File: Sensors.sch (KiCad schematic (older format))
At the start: 5 parts, among them U5 MPRLS0015PA000

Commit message: Correct schematics after review
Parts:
- added C13, C16, C17: 0.1uF, symbol Device:C_Small
- added C14: 1nF, symbol Device:C_Small
- added CONN10: Digital input 1, Molex Picoblade 2 pin, symbol _connectors:CONN_2PIN
- added CONN11: Digital input 2, Molex Picoblade 2 pin, symbol _connectors:CONN_2PIN
- added R6, R7, R8, R9: 10k, symbol Device:R_Small
- added TP1: TestPoint I2C_SDA, symbol Connector:TestPoint
- added TP2: TestPoint I2C_SCL, symbol Connector:TestPoint
- added U6: MPRLS0015PA000, MODULE, symbol _sensors:MPRLS0015PA000
- CONN7, CONN8: value ADC_2PIN -> ADC_2PIN, Molex Picoblade 2 pin
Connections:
- net labels added: DIGITAL_IN1, DIGITAL_IN2, VACUUM_SENS1_RESET, VACUUM_SENS2_RESET
- net labels removed: VACUUM_SENS_RST
- wire segments 9 -> 51
- no-connect marks 5 -> 10
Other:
- note added: "Fc = 318 Hz\n(10k+10k)/(10k*10k*100nF*2*pi)"
- moved on the sheet: C11, C12, CONN7, CONN8, U5

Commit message: Cleanup labels, motor placement, power labels
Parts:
- removed TP1: TestPoint I2C_SDA, symbol Connector:TestPoint
- removed TP2: TestPoint I2C_SCL, symbol Connector:TestPoint
- CONN10, CONN11: symbol _connectors:CONN_2PIN -> actuator-board-rescue:CONN_2PIN-_connectors
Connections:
- net labels added: GND, VCC
- net labels removed: SENSORS_GND, SENSORS_POWER
- wire segments 51 -> 42
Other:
- moved on the sheet: C11, C13, C16, C17, CONN7, CONN8, R6, R7, R8, R9

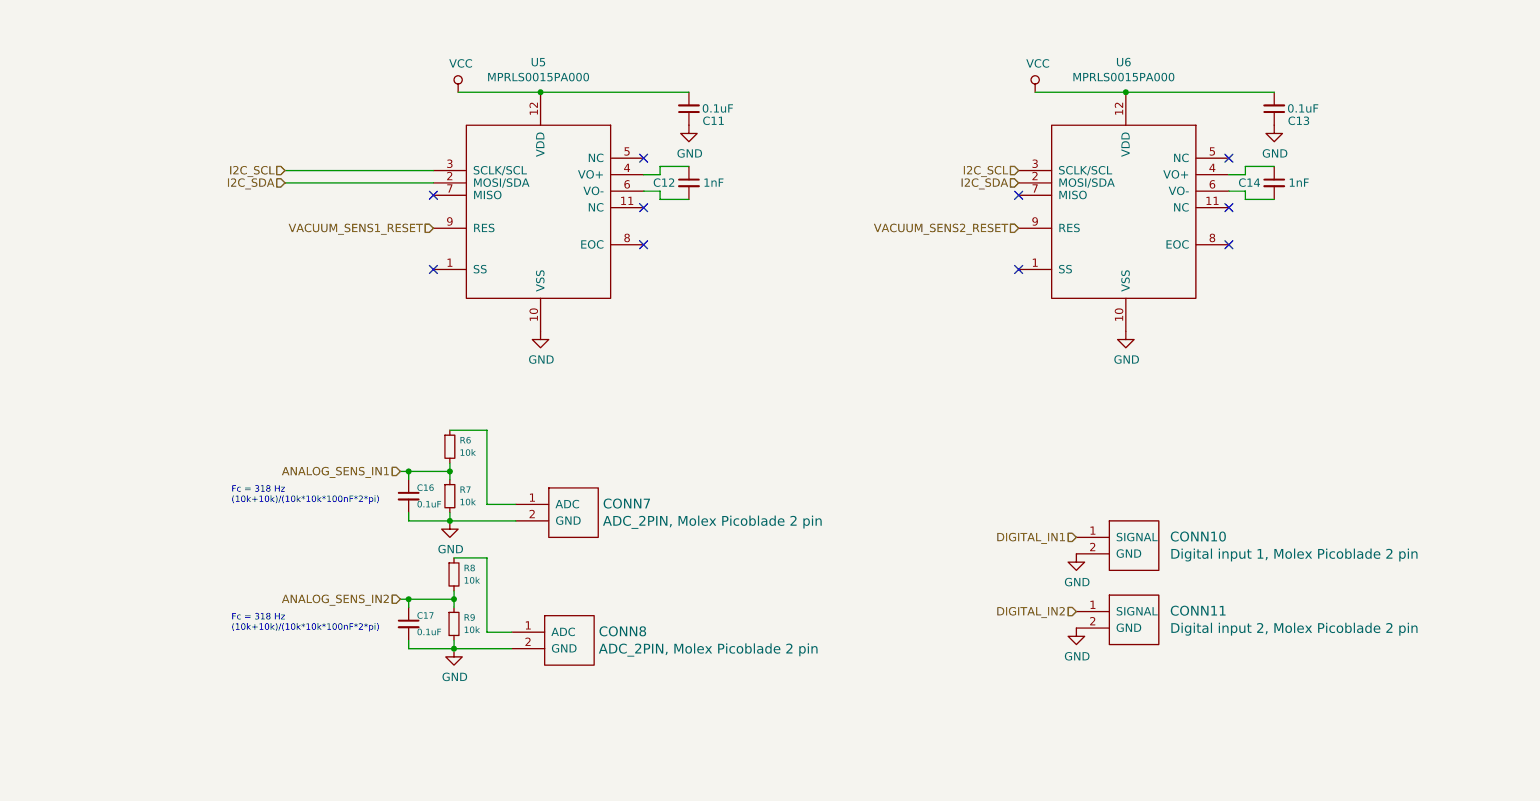
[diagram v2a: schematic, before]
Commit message: Clear component annotation
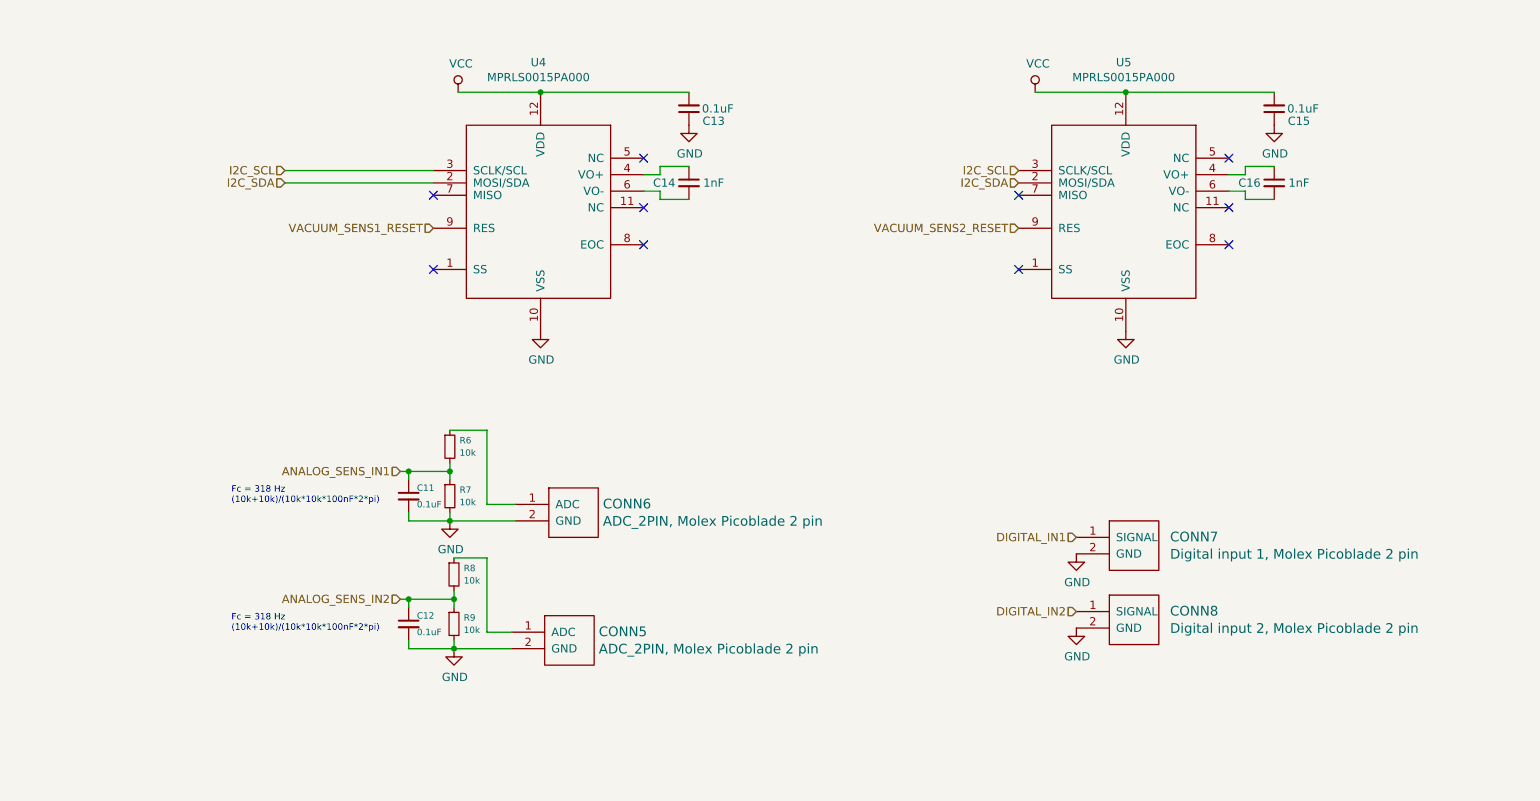
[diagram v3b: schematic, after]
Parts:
- renumbered C16 to C11, C17 to C12, C11 to C13, C12 to C14, C13 to C15, C14 to C16, CONN8 to CONN5, CONN7 to CONN6, CONN10 to CONN7, CONN11 to CONN8, U5 to U4, U6 to U5
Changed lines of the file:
@@
 NoConn ~ 3550 3125
 $Comp
-L Device:C_Small C12
+L Device:C_Small C14
 U 1 1 5E251FA3
 P 5100 2600
-F 0 "C12" H 4950 2600 50  0000 C CNN
+F 0 "C14" H 4950 2600 50  0000 C CNN
 F 1 "1nF" H 5250 2600 50  0000 C CNN
 F 2 "" H 5100 2600 50  0001 C CNN
@@
 NoConn ~ 4825 2975
 $Comp
-L _connectors:ADC_2PIN CONN8
+L _connectors:ADC_2PIN CONN5
 U 1 1 5E2563B4
 P 4375 5725
-F 0 "CONN8" H 4553 6128 59  0000 L CNN
+F 0 "CONN5" H 4553 6128 59  0000 L CNN
 F 1 "ADC_2PIN, Molex Picoblade 2 pin" H 4553 6023 59  0000 L CNN
 F 2 "" H 4375 5725 59  0000 C CNN
@@
 DIGITAL_IN1
 $Comp
-L actuator-board-rescue:CONN_2PIN-_connectors CONN11
+L actuator-board-rescue:CONN_2PIN-_connectors CONN?
 U 1 1 5E2B70AE
 P 7800 5600
-AR Path="/5E2B70AE" Ref="CONN11"  Part="1"
-AR Path="/5E1FAFCF/5E2B70AE" Ref="CONN11"  Part="1"
-F 0 "CONN11" H 8018 6003 59  0000 L CNN
+AR Path="/5E2B70AE" Ref="CONN?"  Part="1"
+AR Path="/5E1FAFCF/5E2B70AE" Ref="CONN8"  Part="1"
+F 0 "CONN8" H 8018 6003 59  0000 L CNN
 F 1 "Digital input 2, Molex Picoblade 2 pin" H 8018 5898 59  0000 L CNN
 F 2 "" H 7800 5600 59  0000 C CNN
@@
 NoConn ~ 7100 3125
 $Comp
-L Device:C_Small C14
+L Device:C_Small C16
 U 1 1 5E2C4BE4
 P 8650 2600
-F 0 "C14" H 8500 2600 50  0000 C CNN
+F 0 "C16" H 8500 2600 50  0000 C CNN
 F 1 "1nF" H 8800 2600 50  0000 C CNN
 F 2 "" H 8650 2600 50  0001 C CNN
@@
 	4200 2050 3700 2050
 $Comp
-L actuator-board-rescue:CONN_2PIN-_connectors CONN10
+L actuator-board-rescue:CONN_2PIN-_connectors CONN?
 U 1 1 5E2B60FB
 P 7800 5150
-AR Path="/5E2B60FB" Ref="CONN10"  Part="1"
-AR Path="/5E1FAFCF/5E2B60FB" Ref="CONN10"  Part="1"
-F 0 "CONN10" H 8018 5553 59  0000 L CNN
+AR Path="/5E2B60FB" Ref="CONN?"  Part="1"
+AR Path="/5E1FAFCF/5E2B60FB" Ref="CONN7"  Part="1"
+F 0 "CONN7" H 8018 5553 59  0000 L CNN
 F 1 "Digital input 1, Molex Picoblade 2 pin" H 8018 5448 59  0000 L CNN
 F 2 "" H 7800 5150 59  0000 C CNN
@@
 $EndComp
 $Comp
-L _sensors:MPRLS0015PA000 U5
+L _sensors:MPRLS0015PA000 U4
 U 1 1 5E2431FF
 P 4200 2850
-F 0 "U5" H 4187 3831 50  0000 C CNN
+F 0 "U4" H 4187 3831 50  0000 C CNN
 F 1 "MPRLS0015PA000" H 4187 3740 50  0000 C CNN
 F 2 "MODULE" H 4300 2200 50  0001 L CNN
@@
 $EndComp
 $Comp
-L Device:C_Small C13
+L Device:C_Small C15
 U 1 1 5E3021F3
 P 8650 2150
-F 0 "C13" H 8500 2225 50  0000 C CNN
+F 0 "C15" H 8500 2225 50  0000 C CNN
 F 1 "0.1uF" H 8475 2150 50  0000 C CNN
 F 2 "" H 8650 2150 50  0001 C CNN
@@
 $EndComp
 $Comp
-L Device:C_Small C16
+L Device:C_Small C11
 U 1 1 5E30FCAA
 P 3400 4500
-F 0 "C16" H 3450 4550 39  0000 L CNN
+F 0 "C11" H 3450 4550 39  0000 L CNN
 F 1 "0.1uF" H 3450 4450 39  0000 L CNN
 F 2 "" H 3400 4500 50  0001 C CNN
@@
 $EndComp
 $Comp
-L Device:C_Small C17
+L Device:C_Small C12
 U 1 1 5E315BCA
 P 3400 5275
-F 0 "C17" H 3450 5325 39  0000 L CNN
+F 0 "C12" H 3450 5325 39  0000 L CNN
 F 1 "0.1uF" H 3450 5225 39  0000 L CNN
 F 2 "" H 3400 5275 50  0001 C CNN
@@
 $EndComp
 $Comp
-L _connectors:ADC_2PIN CONN7
+L _connectors:ADC_2PIN CONN6
 U 1 1 5E255B96
 P 4400 4950
-F 0 "CONN7" H 4578 5353 59  0000 L CNN
+F 0 "CONN6" H 4578 5353 59  0000 L CNN
 F 1 "ADC_2PIN, Molex Picoblade 2 pin" H 4578 5248 59  0000 L CNN
 F 2 "" H 4400 4950 59  0000 C CNN
@@
 	3400 5125 3675 5125
 $Comp
-L power:VCC #PWR0104
+L power:VCC #PWR025
 U 1 1 5E4E3256
 P 3700 2050
-F 0 "#PWR0104" H 3700 1900 50  0001 C CNN
+F 0 "#PWR025" H 3700 1900 50  0001 C CNN
 F 1 "VCC" H 3717 2223 50  0000 C CNN
 F 2 "" H 3700 2050 50  0001 C CNN
@@
 $EndComp
 $Comp
-L power:VCC #PWR0105
+L power:VCC #PWR028
 U 1 1 5E4E76D3
 P 7200 2050
-F 0 "#PWR0105" H 7200 1900 50  0001 C CNN
+F 0 "#PWR028" H 7200 1900 50  0001 C CNN
 F 1 "VCC" H 7217 2223 50  0000 C CNN
 F 2 "" H 7200 2050 50  0001 C CNN
@@
 $EndComp
 $Comp
-L power:GND #PWR0106
+L power:GND #PWR032
 U 1 1 5E4E8303
 P 8650 2250
-F 0 "#PWR0106" H 8650 2000 50  0001 C CNN
+F 0 "#PWR032" H 8650 2000 50  0001 C CNN
 F 1 "GND" H 8655 2077 50  0000 C CNN
 F 2 "" H 8650 2250 50  0001 C CNN
@@
 $EndComp
 $Comp
-L power:GND #PWR0108
+L power:GND #PWR027
 U 1 1 5E4F06AA
 P 5100 2250
-F 0 "#PWR0108" H 5100 2000 50  0001 C CNN
+F 0 "#PWR027" H 5100 2000 50  0001 C CNN
 F 1 "GND" H 5105 2077 50  0000 C CNN
 F 2 "" H 5100 2250 50  0001 C CNN
@@
 $EndComp
 $Comp
-L Device:C_Small C11
+L Device:C_Small C13
 U 1 1 5E250C7A
 P 5100 2150
-F 0 "C11" H 4950 2225 50  0000 C CNN
+F 0 "C13" H 4950 2225 50  0000 C CNN
 F 1 "0.1uF" H 4925 2150 50  0000 C CNN
 F 2 "" H 5100 2150 50  0001 C CNN
@@
 Connection ~ 4200 2050
 $Comp
-L power:GND #PWR0109
+L power:GND #PWR026
 U 1 1 5E4F567D
 P 4200 3500
-F 0 "#PWR0109" H 4200 3250 50  0001 C CNN
+F 0 "#PWR026" H 4200 3250 50  0001 C CNN
 F 1 "GND" H 4205 3327 50  0000 C CNN
 F 2 "" H 4200 3500 50  0001 C CNN
@@
 Connection ~ 7750 2050
 $Comp
-L _sensors:MPRLS0015PA000 U6
+L _sensors:MPRLS0015PA000 U5
 U 1 1 5E2C4BE5
 P 7750 2850
-F 0 "U6" H 7737 3831 50  0000 C CNN
+F 0 "U5" H 7737 3831 50  0000 C CNN
 F 1 "MPRLS0015PA000" H 7737 3740 50  0000 C CNN
 F 2 "MODULE" H 7850 2200 50  0001 L CNN
@@
 $EndComp
 $Comp
-L power:GND #PWR0110
+L power:GND #PWR031
 U 1 1 5E4F5DD6
 P 7750 3500
-F 0 "#PWR0110" H 7750 3250 50  0001 C CNN
+F 0 "#PWR031" H 7750 3250 50  0001 C CNN
 F 1 "GND" H 7755 3327 50  0000 C CNN
 F 2 "" H 7750 3500 50  0001 C CNN
@@
 $EndComp
 $Comp
-L power:GND #PWR0111
+L power:GND #PWR029
 U 1 1 5E4F62EA
 P 7450 4850
-F 0 "#PWR0111" H 7450 4600 50  0001 C CNN
+F 0 "#PWR029" H 7450 4600 50  0001 C CNN
 F 1 "GND" H 7455 4677 50  0000 C CNN
 F 2 "" H 7450 4850 50  0001 C CNN
@@
 $EndComp
 $Comp
-L power:GND #PWR0112
+L power:GND #PWR030
 U 1 1 5E4F6F64
 P 7450 5300
-F 0 "#PWR0112" H 7450 5050 50  0001 C CNN
+F 0 "#PWR030" H 7450 5050 50  0001 C CNN
 F 1 "GND" H 7455 5127 50  0000 C CNN
 F 2 "" H 7450 5300 50  0001 C CNN
@@
 $EndComp
 $Comp
-L power:GND #PWR0113
+L power:GND #PWR023
 U 1 1 5E4F86A7
 P 3650 4650
-F 0 "#PWR0113" H 3650 4400 50  0001 C CNN
+F 0 "#PWR023" H 3650 4400 50  0001 C CNN
 F 1 "GND" H 3655 4477 50  0000 C CNN
 F 2 "" H 3650 4650 50  0001 C CNN
@@
 Connection ~ 3675 5425
 $Comp
-L power:GND #PWR0114
+L power:GND #PWR024
 U 1 1 5E503BBC
 P 3675 5425
-F 0 "#PWR0114" H 3675 5175 50  0001 C CNN
+F 0 "#PWR024" H 3675 5175 50  0001 C CNN
 F 1 "GND" H 3680 5252 50  0000 C CNN
 F 2 "" H 3675 5425 50  0001 C CNN

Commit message: Switch to SPI, fixed sensor and motor driver symbols.
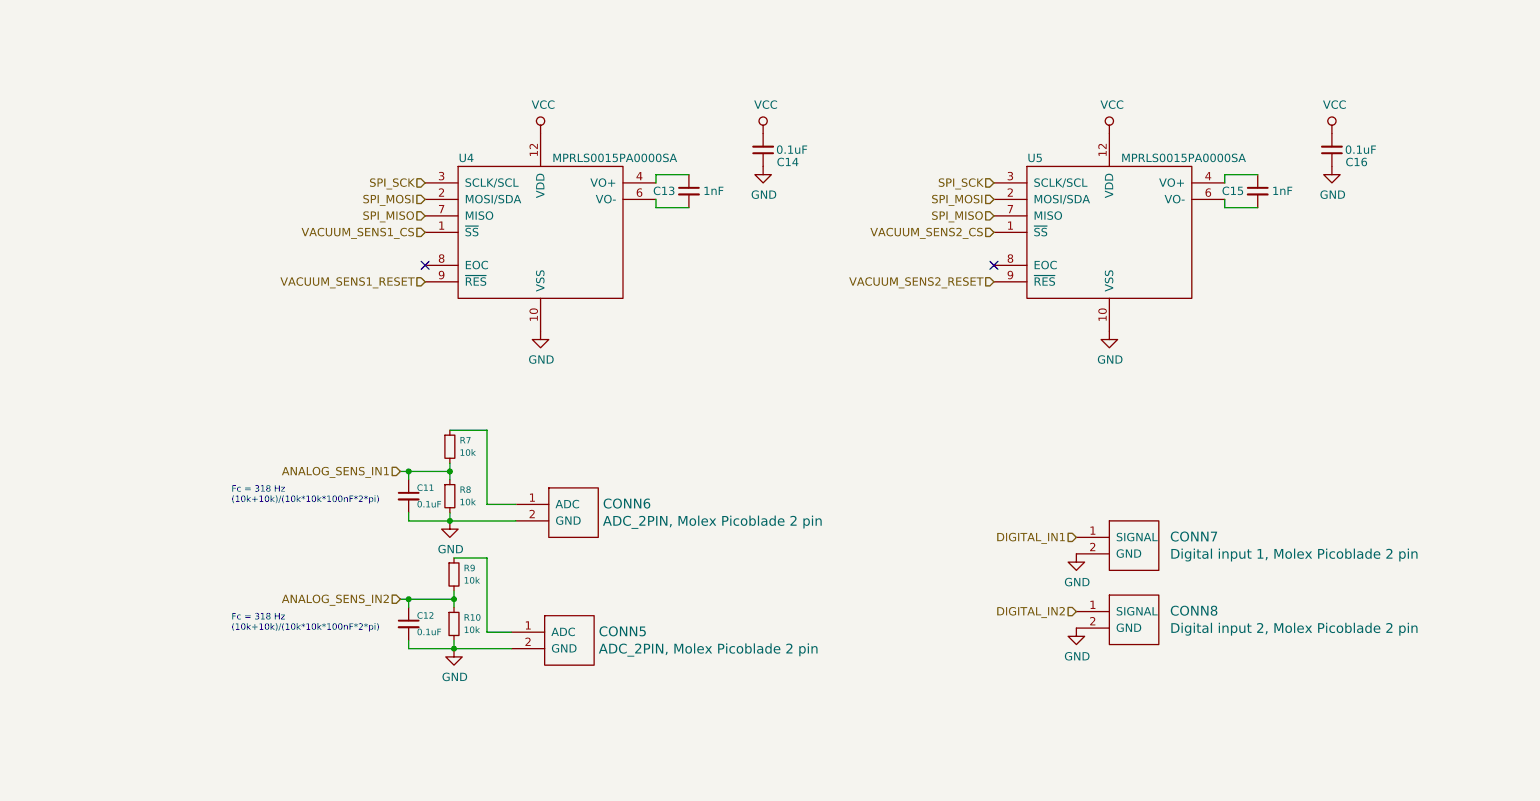
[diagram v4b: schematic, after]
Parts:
- removed U4, U5: MPRLS0015PA000, MODULE, symbol _sensors:MPRLS0015PA000
- added U4, U5: MPRLS0015PA0000SA, MODULE, symbol _sensors:MPRLS0015PA0000SA
- C15: value 0.1uF -> 1nF
- C16: value 1nF -> 0.1uF
- renumbered C14 to C13, C13 to C14, R9 to R10, R6 to R7, R7 to R8, R8 to R9
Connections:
- net GND: now also C16.1, U4.10 (VSS), U5.10 (VSS); no longer C15.1
- net VACUUM_SENS1_RESET: now also U4.9 (~RES)
- net VACUUM_SENS2_RESET: now also U5.9 (~RES)
- net VCC: now also C16.2, U4.12 (VDD), U5.12 (VDD); no longer C15.2
- net at C13.1: now also U4.4 (VO+)
- net at C13.2: now also U4.6 (VO-)
- new net: C15.1, U5.4 (VO+)
- new net: C15.2, U5.6 (VO-)
- new net SPI_MISO: U4.7 (MISO), U5.7 (MISO)
- new net SPI_MOSI: U4.2 (MOSI/SDA), U5.2 (MOSI/SDA)
- new net SPI_SCK: U4.3 (SCLK/SCL), U5.3 (SCLK/SCL)
- new net VACUUM_SENS1_CS: U4.1 (~SS)
- new net VACUUM_SENS2_CS: U5.1 (~SS)
- no-connect marks 10 -> 2
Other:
- moved on the sheet: C13, C14

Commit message: Work on footprint assignment
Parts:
- C11, C12, C13, C14, C15, C16: footprint (none) -> Capacitor_SMD:C_0603_1608Metric
- U4, U5: footprint MODULE -> _sensors:MPR
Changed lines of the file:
@@
 F 0 "CONN5" H 4553 6128 59  0000 L CNN
 F 1 "ADC_2PIN, Molex Picoblade 2 pin" H 4553 6023 59  0000 L CNN
-F 2 "" H 4375 5725 59  0000 C CNN
+F 2 "" H 4375 5725 59  0001 C CNN
 F 3 "" H 4375 5725 59  0000 C CNN
 	1    4375 5725
@@
 F 0 "CONN8" H 8018 6003 59  0000 L CNN
 F 1 "Digital input 2, Molex Picoblade 2 pin" H 8018 5898 59  0000 L CNN
-F 2 "" H 7800 5600 59  0000 C CNN
+F 2 "" H 7800 5600 59  0001 C CNN
 F 3 "" H 7800 5600 59  0000 C CNN
 	1    7800 5600
@@
 F 0 "CONN7" H 8018 5553 59  0000 L CNN
 F 1 "Digital input 1, Molex Picoblade 2 pin" H 8018 5448 59  0000 L CNN
-F 2 "" H 7800 5150 59  0000 C CNN
+F 2 "" H 7800 5150 59  0001 C CNN
 F 3 "" H 7800 5150 59  0000 C CNN
 	1    7800 5150
@@
 F 0 "C11" H 3450 4550 39  0000 L CNN
 F 1 "0.1uF" H 3450 4450 39  0000 L CNN
-F 2 "" H 3400 4500 50  0001 C CNN
+F 2 "Capacitor_SMD:C_0603_1608Metric" H 3400 4500 50  0001 C CNN
 F 3 "~" H 3400 4500 50  0001 C CNN
 	1    3400 4500
@@
 F 0 "C12" H 3450 5325 39  0000 L CNN
 F 1 "0.1uF" H 3450 5225 39  0000 L CNN
-F 2 "" H 3400 5275 50  0001 C CNN
+F 2 "Capacitor_SMD:C_0603_1608Metric" H 3400 5275 50  0001 C CNN
 F 3 "~" H 3400 5275 50  0001 C CNN
 	1    3400 5275
@@
 F 0 "CONN6" H 4578 5353 59  0000 L CNN
 F 1 "ADC_2PIN, Molex Picoblade 2 pin" H 4578 5248 59  0000 L CNN
-F 2 "" H 4400 4950 59  0000 C CNN
+F 2 "" H 4400 4950 59  0001 C CNN
 F 3 "" H 4400 4950 59  0000 C CNN
 	1    4400 4950
@@
 F 0 "C14" H 5400 2475 50  0000 C CNN
 F 1 "0.1uF" H 5375 2400 50  0000 C CNN
-F 2 "" H 5550 2400 50  0001 C CNN
+F 2 "Capacitor_SMD:C_0603_1608Metric" H 5550 2400 50  0001 C CNN
 F 3 "~" H 5550 2400 50  0001 C CNN
 	1    5550 2400
@@
 F 0 "U4" H 3750 3350 50  0000 C CNN
 F 1 "MPRLS0015PA0000SA" H 4650 3350 50  0000 C CNN
-F 2 "MODULE" H 4200 2900 50  0001 L CNN
+F 2 "_sensors:MPR" H 4200 2900 50  0001 L CNN
 F 3 "https://sensing.honeywell.com/honeywell-sensing-micropressure-board-mount-pressure-mpr-series-datasheet-32332628.pdf" H 4300 2275 50  0001 L CNN
 	1    4200 2900
@@
 F 0 "C13" H 4950 2650 50  0000 C CNN
 F 1 "1nF" H 5250 2650 50  0000 C CNN
-F 2 "" H 5100 2650 50  0001 C CNN
+F 2 "Capacitor_SMD:C_0603_1608Metric" H 5100 2650 50  0001 C CNN
 F 3 "~" H 5100 2650 50  0001 C CNN
 	1    5100 2650
@@
 F 0 "C16" H 8850 2475 50  0000 C CNN
 F 1 "0.1uF" H 8825 2400 50  0000 C CNN
-F 2 "" H 9000 2400 50  0001 C CNN
+F 2 "Capacitor_SMD:C_0603_1608Metric" H 9000 2400 50  0001 C CNN
 F 3 "~" H 9000 2400 50  0001 C CNN
 	1    9000 2400
@@
 F 0 "U5" H 7200 3350 50  0000 C CNN
 F 1 "MPRLS0015PA0000SA" H 8100 3350 50  0000 C CNN
-F 2 "MODULE" H 7650 2900 50  0001 L CNN
+F 2 "_sensors:MPR" H 7650 2900 50  0001 L CNN
 F 3 "https://sensing.honeywell.com/honeywell-sensing-micropressure-board-mount-pressure-mpr-series-datasheet-32332628.pdf" H 7750 2275 50  0001 L CNN
 	1    7650 2900
@@
 F 0 "C15" H 8400 2650 50  0000 C CNN
 F 1 "1nF" H 8700 2650 50  0000 C CNN
-F 2 "" H 8550 2650 50  0001 C CNN
+F 2 "Capacitor_SMD:C_0603_1608Metric" H 8550 2650 50  0001 C CNN
 F 3 "~" H 8550 2650 50  0001 C CNN
 	1    8550 2650
